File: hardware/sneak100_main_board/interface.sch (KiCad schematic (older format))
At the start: 13 parts

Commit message: Proximity sensor first test
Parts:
- gave numbers to parts that had none: 13
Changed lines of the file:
@@
 $EndDescr
 $Comp
-L Switch:SW_Push SW?
+L Switch:SW_Push SW1
 U 1 1 61053EFA
 P 1950 1650
-F 0 "SW?" H 1950 1935 50  0000 C CNN
+F 0 "SW1" H 1950 1935 50  0000 C CNN
 F 1 "SW_Push" H 1950 1844 50  0000 C CNN
 F 2 "" H 1950 1850 50  0001 C CNN
@@
 $EndComp
 $Comp
-L Device:R R?
+L Device:R R1
 U 1 1 61055001
 P 2200 1450
-F 0 "R?" H 2270 1496 50  0000 L CNN
+F 0 "R1" H 2270 1496 50  0000 L CNN
 F 1 "4k7" H 2270 1405 50  0000 L CNN
 F 2 "" V 2130 1450 50  0001 C CNN
@@
 $EndComp
 $Comp
-L power:+3.3V #PWR?
+L power:+3.3V #PWR01
 U 1 1 610558C1
 P 2200 1300
-F 0 "#PWR?" H 2200 1150 50  0001 C CNN
+F 0 "#PWR01" H 2200 1150 50  0001 C CNN
 F 1 "+3.3V" H 2215 1473 50  0000 C CNN
 F 2 "" H 2200 1300 50  0001 C CNN
@@
 $EndComp
 $Comp
-L power:GND #PWR?
+L power:GND #PWR03
 U 1 1 61055FD5
 P 1700 1700
-F 0 "#PWR?" H 1700 1450 50  0001 C CNN
+F 0 "#PWR03" H 1700 1450 50  0001 C CNN
 F 1 "GND" H 1705 1527 50  0000 C CNN
 F 2 "" H 1700 1700 50  0001 C CNN
@@
 $EndComp
 $Comp
-L Device:C C?
+L Device:C C1
 U 1 1 61056486
 P 2200 1850
-F 0 "C?" H 2315 1896 50  0000 L CNN
+F 0 "C1" H 2315 1896 50  0000 L CNN
 F 1 "100nF" H 2315 1805 50  0000 L CNN
 F 2 "" H 2238 1700 50  0001 C CNN
@@
 $EndComp
 $Comp
-L power:GND #PWR?
+L power:GND #PWR05
 U 1 1 6105698D
 P 2200 2000
-F 0 "#PWR?" H 2200 1750 50  0001 C CNN
+F 0 "#PWR05" H 2200 1750 50  0001 C CNN
 F 1 "GND" H 2205 1827 50  0000 C CNN
 F 2 "" H 2200 2000 50  0001 C CNN
@@
 BUTTON1
 $Comp
-L Switch:SW_Push SW?
+L Switch:SW_Push SW2
 U 1 1 6105C05B
 P 3250 1650
-F 0 "SW?" H 3250 1935 50  0000 C CNN
+F 0 "SW2" H 3250 1935 50  0000 C CNN
 F 1 "SW_Push" H 3250 1844 50  0000 C CNN
 F 2 "" H 3250 1850 50  0001 C CNN
@@
 $EndComp
 $Comp
-L Device:R R?
+L Device:R R2
 U 1 1 6105C061
 P 3500 1450
-F 0 "R?" H 3570 1496 50  0000 L CNN
+F 0 "R2" H 3570 1496 50  0000 L CNN
 F 1 "4k7" H 3570 1405 50  0000 L CNN
 F 2 "" V 3430 1450 50  0001 C CNN
@@
 $EndComp
 $Comp
-L power:+3.3V #PWR?
+L power:+3.3V #PWR02
 U 1 1 6105C067
 P 3500 1300
-F 0 "#PWR?" H 3500 1150 50  0001 C CNN
+F 0 "#PWR02" H 3500 1150 50  0001 C CNN
 F 1 "+3.3V" H 3515 1473 50  0000 C CNN
 F 2 "" H 3500 1300 50  0001 C CNN
@@
 $EndComp
 $Comp
-L power:GND #PWR?
+L power:GND #PWR04
 U 1 1 6105C06D
 P 3000 1700
-F 0 "#PWR?" H 3000 1450 50  0001 C CNN
+F 0 "#PWR04" H 3000 1450 50  0001 C CNN
 F 1 "GND" H 3005 1527 50  0000 C CNN
 F 2 "" H 3000 1700 50  0001 C CNN
@@
 $EndComp
 $Comp
-L Device:C C?
+L Device:C C2
 U 1 1 6105C073
 P 3500 1850
-F 0 "C?" H 3615 1896 50  0000 L CNN
+F 0 "C2" H 3615 1896 50  0000 L CNN
 F 1 "100nF" H 3615 1805 50  0000 L CNN
 F 2 "" H 3538 1700 50  0001 C CNN
@@
 $EndComp
 $Comp
-L power:GND #PWR?
+L power:GND #PWR06
 U 1 1 6105C079
 P 3500 2000
-F 0 "#PWR?" H 3500 1750 50  0001 C CNN
+F 0 "#PWR06" H 3500 1750 50  0001 C CNN
 F 1 "GND" H 3505 1827 50  0000 C CNN
 F 2 "" H 3500 2000 50  0001 C CNN
@@
 BUTTON2
 $Comp
-L Device:LED D?
+L Device:LED D1
 U 1 1 6105F07D
 P 1900 2900
-F 0 "D?" H 1893 2645 50  0000 C CNN
+F 0 "D1" H 1893 2645 50  0000 C CNN
 F 1 "LED" H 1893 2736 50  0000 C CNN
 F 2 "" H 1900 2900 50  0001 C CNN
@@
 $EndComp
 $Comp
-L Device:R R?
+L Device:R R3
 U 1 1 61060DB0
 P 1600 2900
-F 0 "R?" V 1393 2900 50  0000 C CNN
+F 0 "R3" V 1393 2900 50  0000 C CNN
 F 1 "300" V 1484 2900 50  0000 C CNN
 F 2 "" V 1530 2900 50  0001 C CNN
@@
 $EndComp
 $Comp
-L power:GND #PWR?
+L power:GND #PWR07
 U 1 1 61061E6F
 P 2050 2900
-F 0 "#PWR?" H 2050 2650 50  0001 C CNN
+F 0 "#PWR07" H 2050 2650 50  0001 C CNN
 F 1 "GND" V 2055 2772 50  0000 R CNN
 F 2 "" H 2050 2900 50  0001 C CNN
@@
 Green led current resistor calculations:\n\ntarget current: I = 5mA\ninput voltage: U = 3.3V\nforward voltage: Uf = 2V\n\nR = (U-Uf)/I\nR = (3.3 -2.9)/0.005 = 260ohm -> 300ohm
 $Comp
-L Device:LED D?
+L Device:LED D2
 U 1 1 61066928
 P 1900 3300
-F 0 "D?" H 1893 3045 50  0000 C CNN
+F 0 "D2" H 1893 3045 50  0000 C CNN
 F 1 "LED" H 1893 3136 50  0000 C CNN
 F 2 "" H 1900 3300 50  0001 C CNN
@@
 $EndComp
 $Comp
-L Device:R R?
+L Device:R R4
 U 1 1 6106692E
 P 1600 3300
-F 0 "R?" V 1393 3300 50  0000 C CNN
+F 0 "R4" V 1393 3300 50  0000 C CNN
 F 1 "300" V 1484 3300 50  0000 C CNN
 F 2 "" V 1530 3300 50  0001 C CNN
@@
 $EndComp
 $Comp
-L power:GND #PWR?
+L power:GND #PWR08
 U 1 1 61066934
 P 2050 3300
-F 0 "#PWR?" H 2050 3050 50  0001 C CNN
+F 0 "#PWR08" H 2050 3050 50  0001 C CNN
 F 1 "GND" V 2055 3172 50  0000 R CNN
 F 2 "" H 2050 3300 50  0001 C CNN
@@
 LED2
 $Comp
-L Device:LED D?
+L Device:LED D3
 U 1 1 61067344
 P 1900 3700
-F 0 "D?" H 1893 3445 50  0000 C CNN
+F 0 "D3" H 1893 3445 50  0000 C CNN
 F 1 "LED" H 1893 3536 50  0000 C CNN
 F 2 "" H 1900 3700 50  0001 C CNN
@@
 $EndComp
 $Comp
-L Device:R R?
+L Device:R R5
 U 1 1 6106734A
 P 1600 3700
-F 0 "R?" V 1393 3700 50  0000 C CNN
+F 0 "R5" V 1393 3700 50  0000 C CNN
 F 1 "300" V 1484 3700 50  0000 C CNN
 F 2 "" V 1530 3700 50  0001 C CNN
@@
 $EndComp
 $Comp
-L power:GND #PWR?
+L power:GND #PWR09
 U 1 1 61067350
 P 2050 3700
-F 0 "#PWR?" H 2050 3450 50  0001 C CNN
+F 0 "#PWR09" H 2050 3450 50  0001 C CNN
 F 1 "GND" V 2055 3572 50  0000 R CNN
 F 2 "" H 2050 3700 50  0001 C CNN
@@
 LED3
 $Comp
-L Connector_Generic:Conn_01x03 J?
+L Connector_Generic:Conn_01x03 J1
 U 1 1 6106D8EA
 P 2950 4800
-F 0 "J?" H 3030 4842 50  0000 L CNN
+F 0 "J1" H 3030 4842 50  0000 L CNN
 F 1 "Conn_01x03" H 3030 4751 50  0000 L CNN
 F 2 "" H 2950 4800 50  0001 C CNN
@@
 $EndComp
 $Comp
-L power:GND #PWR?
+L power:GND #PWR010
 U 1 1 610711F8
 P 2750 4900
-F 0 "#PWR?" H 2750 4650 50  0001 C CNN
+F 0 "#PWR010" H 2750 4650 50  0001 C CNN
 F 1 "GND" V 2755 4772 50  0000 R CNN
 F 2 "" H 2750 4900 50  0001 C CNN

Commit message: motors circuit scheme
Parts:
- C1, C2: footprint (none) -> Capacitor_SMD:C_0805_2012Metric
- D1, D2, D3: footprint (none) -> LED_SMD:LED_0805_2012Metric
- J2: renamed from J1; footprint (none) -> Connector_PinHeader_2.54mm:PinHeader_1x03_P2.54mm_Vertical
- R1, R2, R3, R4, R5: footprint (none) -> Resistor_SMD:R_0805_2012Metric
- SW1, SW2: footprint (none) -> Button_Switch_SMD:SW_SPST_FSMSM
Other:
- note added: "User interface"
- moved on the sheet: C1, C2, D1, D2, D3, J2, R1, R2, R3, R4, R5, SW1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

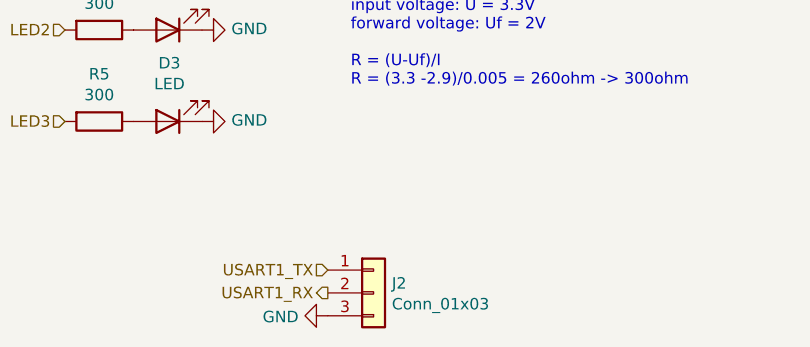
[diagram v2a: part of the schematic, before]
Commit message: Add stm32f405 uC scheme
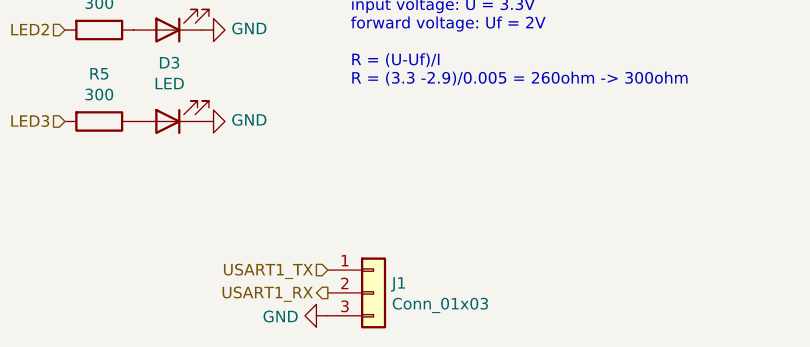
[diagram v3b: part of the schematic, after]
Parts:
- renumbered J2 to J1
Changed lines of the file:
@@
 $Descr A4 11693 8268
 encoding utf-8
-Sheet 3 7
+Sheet 2 7
 Title ""
 Date ""
@@
 LED3
 $Comp
-L Connector_Generic:Conn_01x03 J2
+L Connector_Generic:Conn_01x03 J1
 U 1 1 6106D8EA
 P 3100 4650
-F 0 "J2" H 3180 4692 50  0000 L CNN
+F 0 "J1" H 3180 4692 50  0000 L CNN
 F 1 "Conn_01x03" H 3180 4601 50  0000 L CNN
 F 2 "Connector_PinHeader_2.54mm:PinHeader_1x03_P2.54mm_Vertical" H 3100 4650 50  0001 C CNN

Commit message: Hardware configuration schematic
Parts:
- removed J1: Conn_01x03, Connector_PinHeader_2.54mm:PinHeader_1x03_P2.54mm_Vertical, symbol Connector_Generic:Conn_01x03
- added C3: 4.7uF, Capacitor_SMD:CP_Elec_4x3, symbol Device:CP
- added J1: USB_OTG, Connector_USB:USB_Micro-B_Molex_47346-0001, symbol Connector:USB_OTG
- added J2: Conn_01x06, Connector_PinSocket_2.54mm:PinSocket_1x06_P2.54mm_Vertical, symbol Connector_Generic:Conn_01x06
- added J3: Conn_01x04, Connector_PinSocket_2.54mm:PinSocket_1x04_P2.54mm_Vertical, symbol Connector_Generic:Conn_01x04
- added J4: Conn_01x02, Connector_PinHeader_2.54mm:PinHeader_1x02_P2.54mm_Vertical, symbol Connector_Generic:Conn_01x02
- added R6: 100, Resistor_SMD:R_0805_2012Metric, symbol Device:R
- added R7: 10k, Resistor_SMD:R_0805_2012Metric, symbol Device:R
- added R8, R9: 22, Resistor_SMD:R_0805_2012Metric, symbol Device:R
- added U1: TSOP4838, Connector_PinHeader_2.54mm:PinHeader_1x03_P2.54mm_Vertical, symbol Sneak100_kicad:TSOP4838
- renumbered R3 to R1, R1 to R2, R2 to R3
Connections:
- net +3V3: now also C3.1, J3.1 (Pin_1), R6.1, R7.1
- net GND: now also C3.2, J1.5 (GND), J2.3 (Pin_3), J3.2 (Pin_2), U1.2 (GND)
- new net: J1.2 (D-), R9.1
- new net: J1.3 (D+), R8.2
- new net: R6.2, U1.3 (Vs)
- new net +5V: J2.2 (Pin_2)
- new net BLUETOOTH_RX: J2.5 (Pin_5)
- new net BLUETOOTH_TX: J2.4 (Pin_4)
- new net I2C_SCL: J4.2 (Pin_2)
- new net I2C_SDA: J4.1 (Pin_1)
- new net MODULE_KILL: J3.4 (Pin_4)
- new net MODULE_START: J3.3 (Pin_3)
- new net RECEIVER_OUT: R7.2, U1.1 (OUT)
- new net USB_DM: R9.2
- new net USB_DP: R8.1
- no-connect marks 0 -> 5
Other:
- note added: "For future use:\n- IMU\n- OLED display"
- note added: "I2C bus"
- note added: "IR receiver"
- note added: "USB connection"
- note added: "bluetooth module"
- note added: "start module"
- note added: "user buttons"
- note added: "user leds"
- note removed: "User interface"
- moved on the sheet: C1, C2, D1, D2, D3, R1, R2, R3, R4, R5, SW1, SW2

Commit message: Change usb connector footprint
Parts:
- J1: footprint Connector_USB:USB_Micro-B_Molex_47346-0001 -> Connector_USB:USB_Mini-B_Lumberg_2486_01_Horizontal
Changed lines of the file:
@@
 F 0 "J1" H 2257 4417 50  0000 C CNN
 F 1 "USB_OTG" H 2257 4326 50  0000 C CNN
-F 2 "Connector_USB:USB_Micro-B_Molex_47346-0001" H 2350 3900 50  0001 C CNN
+F 2 "Connector_USB:USB_Mini-B_Lumberg_2486_01_Horizontal" H 2350 3900 50  0001 C CNN
 F 3 " ~" H 2350 3900 50  0001 C CNN
 	1    2200 3950

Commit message: Power section scheme
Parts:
- C1, C2: footprint Capacitor_SMD:C_0805_2012Metric -> Capacitor_SMD:C_0603_1608Metric
- D1, D2, D3: footprint LED_SMD:LED_0805_2012Metric -> LED_SMD:LED_0603_1608Metric
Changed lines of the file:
@@
 F 0 "C1" H 2315 2196 50  0000 L CNN
 F 1 "100nF" H 2315 2105 50  0000 L CNN
-F 2 "Capacitor_SMD:C_0805_2012Metric" H 2238 2000 50  0001 C CNN
+F 2 "Capacitor_SMD:C_0603_1608Metric" H 2238 2000 50  0001 C CNN
 F 3 "~" H 2200 2150 50  0001 C CNN
 	1    2200 2150
@@
 F 0 "C2" H 3615 2196 50  0000 L CNN
 F 1 "100nF" H 3615 2105 50  0000 L CNN
-F 2 "Capacitor_SMD:C_0805_2012Metric" H 3538 2000 50  0001 C CNN
+F 2 "Capacitor_SMD:C_0603_1608Metric" H 3538 2000 50  0001 C CNN
 F 3 "~" H 3500 2150 50  0001 C CNN
 	1    3500 2150
@@
 F 0 "D1" H 6443 1395 50  0000 C CNN
 F 1 "LED" H 6443 1486 50  0000 C CNN
-F 2 "LED_SMD:LED_0805_2012Metric" H 6450 1650 50  0001 C CNN
+F 2 "LED_SMD:LED_0603_1608Metric" H 6450 1650 50  0001 C CNN
 F 3 "~" H 6450 1650 50  0001 C CNN
 	1    6450 1650
@@
 F 0 "D2" H 6443 1795 50  0000 C CNN
 F 1 "LED" H 6443 1886 50  0000 C CNN
-F 2 "LED_SMD:LED_0805_2012Metric" H 6450 2050 50  0001 C CNN
+F 2 "LED_SMD:LED_0603_1608Metric" H 6450 2050 50  0001 C CNN
 F 3 "~" H 6450 2050 50  0001 C CNN
 	1    6450 2050
@@
 F 0 "D3" H 6443 2195 50  0000 C CNN
 F 1 "LED" H 6443 2286 50  0000 C CNN
-F 2 "LED_SMD:LED_0805_2012Metric" H 6450 2450 50  0001 C CNN
+F 2 "LED_SMD:LED_0603_1608Metric" H 6450 2450 50  0001 C CNN
 F 3 "~" H 6450 2450 50  0001 C CNN
 	1    6450 2450

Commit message: USB FDU mode
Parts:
- R23: renamed from R1; footprint Resistor_SMD:R_0805_2012Metric -> Resistor_SMD:R_0603_1608Metric
- R24: renamed from R2; footprint Resistor_SMD:R_0805_2012Metric -> Resistor_SMD:R_0603_1608Metric
- R25: renamed from R3; footprint Resistor_SMD:R_0805_2012Metric -> Resistor_SMD:R_0603_1608Metric
- R26: renamed from R4; footprint Resistor_SMD:R_0805_2012Metric -> Resistor_SMD:R_0603_1608Metric
- R27: renamed from R5; footprint Resistor_SMD:R_0805_2012Metric -> Resistor_SMD:R_0603_1608Metric
- R28: renamed from R6; footprint Resistor_SMD:R_0805_2012Metric -> Resistor_SMD:R_0603_1608Metric
- R29: renamed from R7; footprint Resistor_SMD:R_0805_2012Metric -> Resistor_SMD:R_0603_1608Metric
- R30: renamed from R8; footprint Resistor_SMD:R_0805_2012Metric -> Resistor_SMD:R_0603_1608Metric
- R31: renamed from R9; footprint Resistor_SMD:R_0805_2012Metric -> Resistor_SMD:R_0603_1608Metric
- renumbered C1 to C28, C2 to C29, C3 to C30, D2 to D10, D3 to D11, D1 to D9, J1 to J11, J2 to J12, J3 to J13, J4 to J14, SW1 to SW3, SW2 to SW4, U1 to U9

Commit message: Layout progress
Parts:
- removed C29: 100nF, Capacitor_SMD:C_0603_1608Metric, symbol Device:C
- removed J13: Conn_01x04, Connector_PinSocket_2.54mm:PinSocket_1x04_P2.54mm_Vertical, symbol Connector_Generic:Conn_01x04
- removed R25: 4k7, Resistor_SMD:R_0603_1608Metric, symbol Device:R
- removed SW4: SW_Push, Button_Switch_SMD:SW_SPST_FSMSM, symbol Switch:SW_Push
- C17: renamed from C30; footprint Capacitor_SMD:CP_Elec_4x3 -> Capacitor_THT:CP_Radial_D5.0mm_P2.00mm
- renumbered C28 to C16, J14 to J13, R23 to R19, R24 to R20, R26 to R21, R27 to R22, R28 to R23, R29 to R24, R30 to R25, R31 to R26, SW3 to SW2, U9 to U8
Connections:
- net BUTTON1 renamed BUTTON
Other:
- note added: "user button"
- note removed: "start module"
- note removed: "user buttons"
- moved on the sheet: C16, R20, SW2
